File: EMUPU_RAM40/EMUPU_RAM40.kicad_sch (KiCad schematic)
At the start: 30 parts, among them J1 Conn_01x20_Socket, J2 Conn_01x20_Socket, J3 Barrel_Jack_Switch, J4 Conn_01x06_Pin, J5 Conn_01x08_Pin, SW1 SW_SPDT, SW2 SW_SPST, U1 PIC18F47Q43-IP, U2 628128

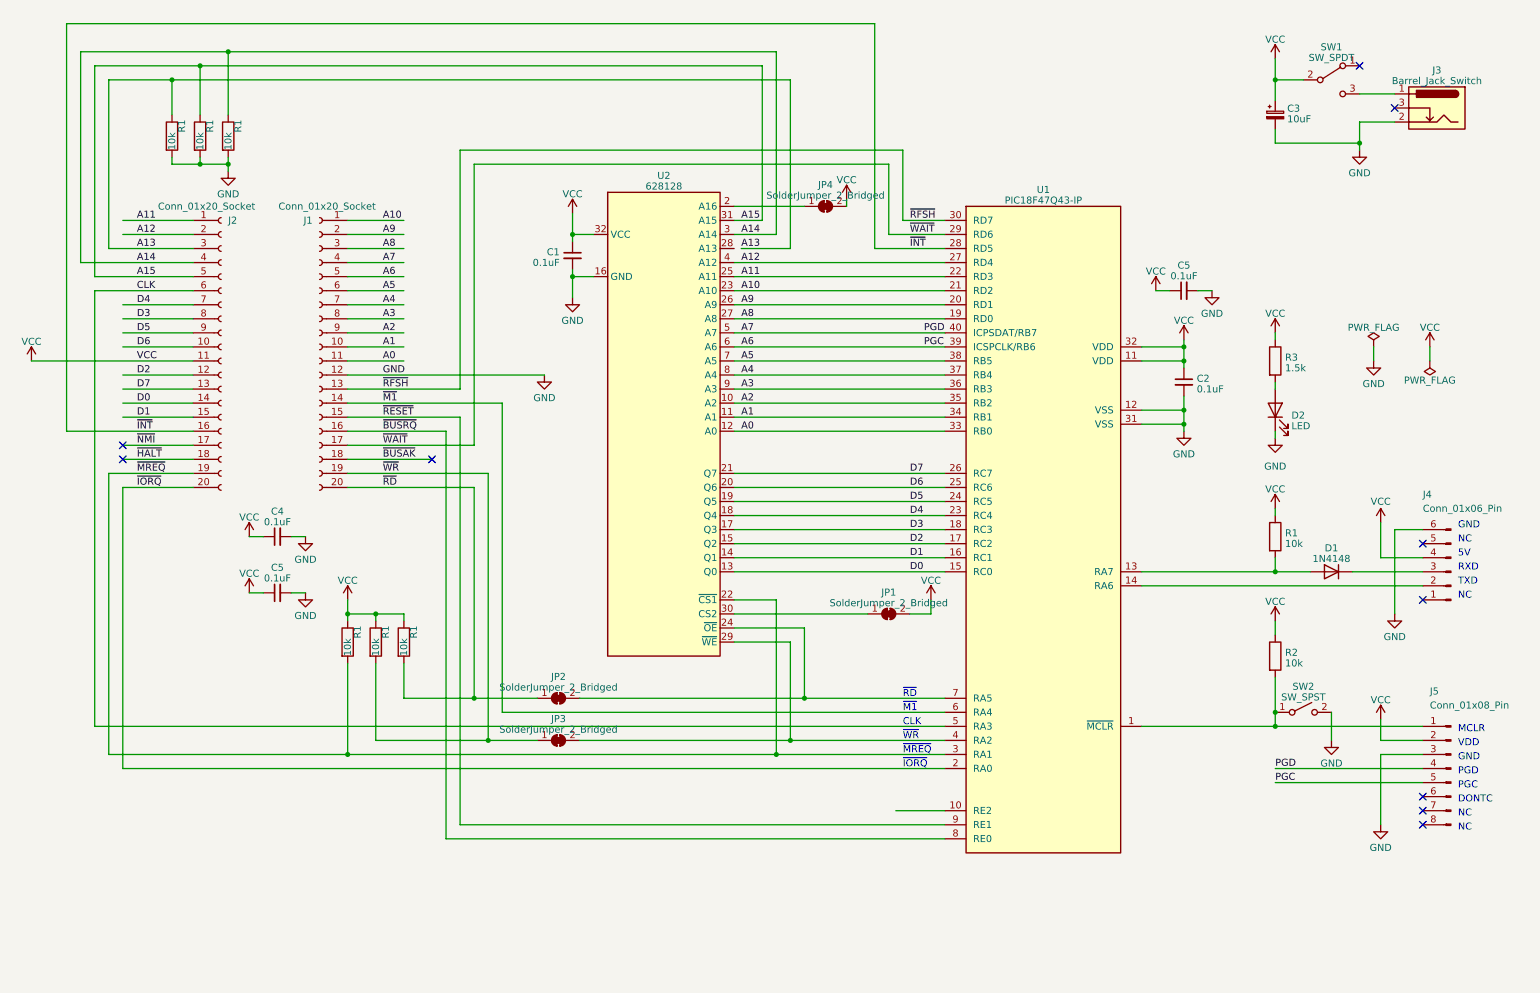
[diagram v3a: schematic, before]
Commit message: Rev003: arrange new footprints, before autorouting
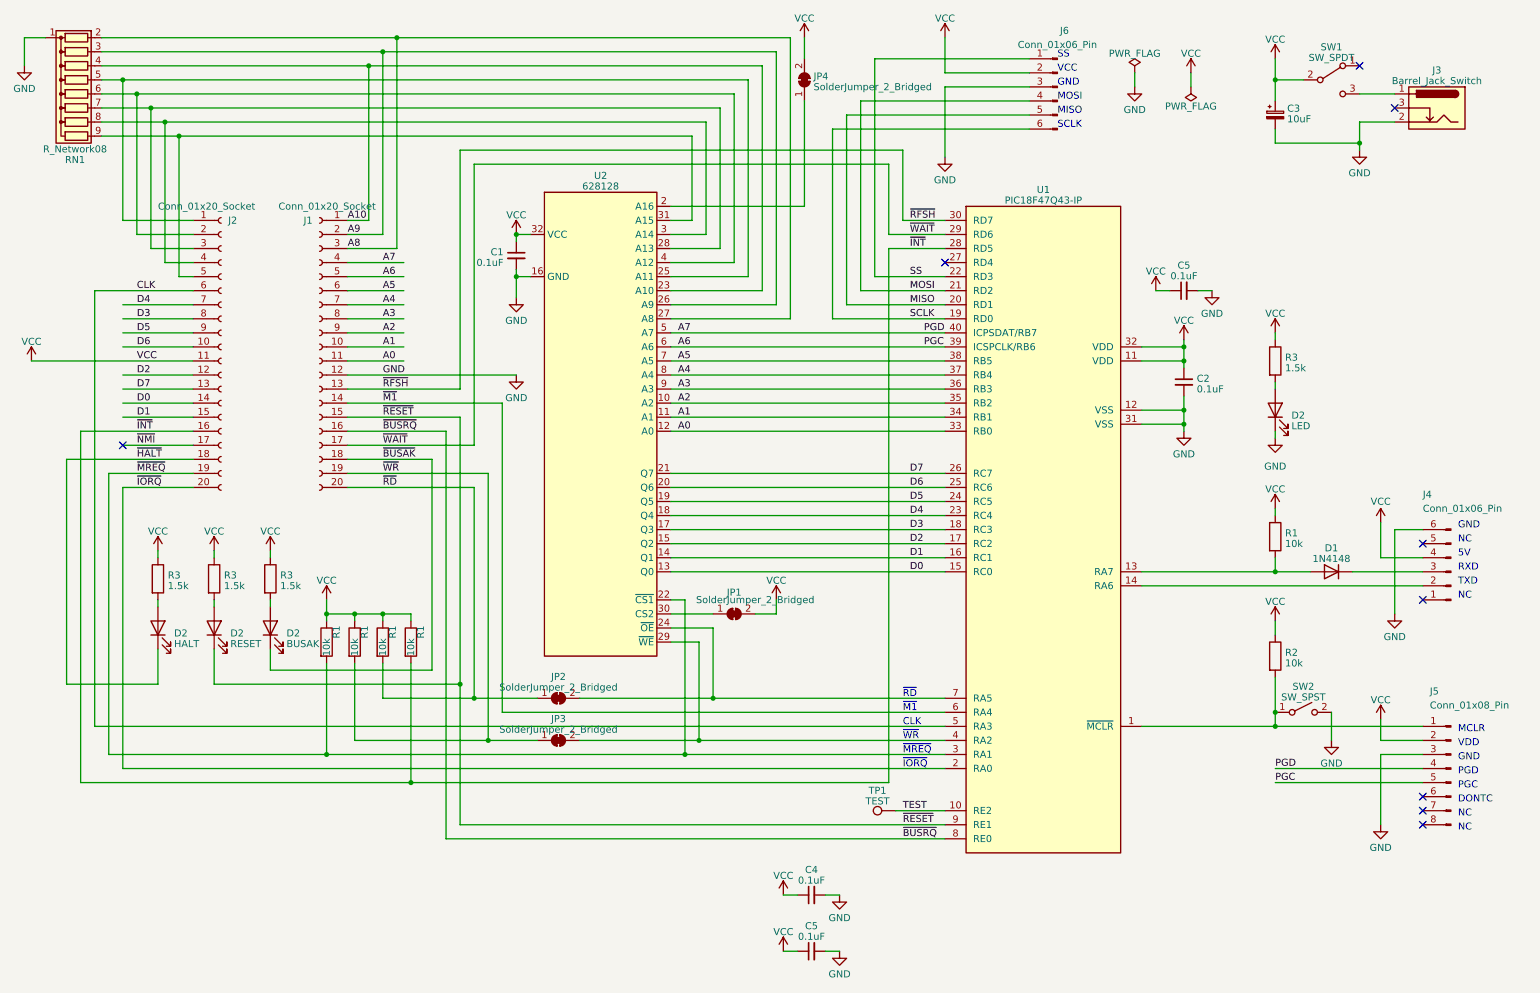
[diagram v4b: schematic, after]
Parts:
- removed R1 (x3): 10k, Resistor_THT:R_Axial_DIN0204_L3.6mm_D1.6mm_P7.62mm_Horizontal, symbol Device:R
- added D2: BUSAK, LED_THT:LED_D3.0mm, symbol Device:LED
- added D2: RESET, LED_THT:LED_D3.0mm, symbol Device:LED
- added D2: HALT, LED_THT:LED_D3.0mm, symbol Device:LED
- added J6: Conn_01x06_Pin, Connector_PinHeader_2.54mm:PinHeader_1x06_P2.54mm_Vertical, symbol Connector:Conn_01x06_Pin
- added R1: 10k, Resistor_THT:R_Axial_DIN0204_L3.6mm_D1.6mm_P7.62mm_Horizontal, symbol Device:R
- added R3 (x3): 1.5k, Resistor_THT:R_Axial_DIN0204_L3.6mm_D1.6mm_P7.62mm_Horizontal, symbol Device:R
- added RN1: R_Network08, Resistor_THT:R_Array_SIP9, symbol Device:R_Network08
- added TP1: TEST, Connector_PinHeader_2.54mm:PinHeader_1x01_P2.54mm_Vertical, symbol Connector:TestPoint
- J3: footprint 0-local:BARREL_JACK -> 0-Project:BARREL_JACK
- J4: footprint 0-local:PinHeader_1x06_P2.54mm_Horizontal_NoFeet -> 0-Project:PinHeader_1x06_P2.54mm_Horizontal_NoFeet
- J5: footprint 0-local:PinHeader_1x08_P2.54mm_Rev_Horizontal_Nofoot -> 0-Project:PinHeader_1x08_P2.54mm_Rev_Horizontal_Nofoot
- SW1: footprint 0-local:PowerSW_for_SBC_series -> 0-Project:PowerSW_for_SBC_series
- SW2: footprint 0-local:SW_PUSH_6mm_H4.3mm -> 0-Project:SW_PUSH_6mm_H4.3mm
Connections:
- net A13 is gone; now on an unnamed net: J2.3 (Pin_3)
- net A10: now also RN1.4 (R3); no longer U1.21 (RD2)
- net A8: now also RN1.2 (R1); no longer U1.19 (RD0)
- net A9: now also RN1.3 (R2); no longer U1.20 (RD1)
- net GND: now also J6.3 (Pin_3), RN1.1 (common)
- net VCC: now also J6.2 (Pin_2), R1.1, R3.1, R3.1, R3.1
- net ~{BUSAK}: now also D2.1 (K)
- net ~{HALT}: now also D2.1 (K)
- net ~{INT}: now also R1.2
- net ~{RESET}: now also D2.1 (K)
- net at U2.28 (A13): now also RN1.7 (R6)
- net TEST: now reaches U1.10 (RE2)
- net TEST: now also TP1.1
- net A11: no longer names the net of J2.1 (Pin_1), U2.25 (A11)
- net A11: now also RN1.5 (R4); no longer U1.22 (RD3)
- net A12: no longer names the net of J2.2 (Pin_2), U2.4 (A12)
- net A12: now also RN1.6 (R5); no longer U1.27 (RD4)
- net A14: no longer names the net of J2.4 (Pin_4), U2.3 (A14)
- net A14: now also RN1.8 (R7)
- net A15: no longer names the net of J2.5 (Pin_5), U2.31 (A15)
- net A15: now also RN1.9 (R8)
- new net: D2.2 (A), R3.2 (x3)
- new net MISO: J6.5 (Pin_5), U1.20 (RD1)
- new net MOSI: J6.4 (Pin_4), U1.21 (RD2)
- new net SCLK: J6.6 (Pin_6), U1.19 (RD0)
- new net SS: J6.1 (Pin_1), U1.22 (RD3)
- no-connect marks 10 -> 9
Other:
- note added: "MISO"
- note added: "MOSI"
- note added: "SCLK"
- note added: "SS"
- note added: "VCC"
- moved on the sheet: C1, C4, C5, JP1, JP4, R1, U2

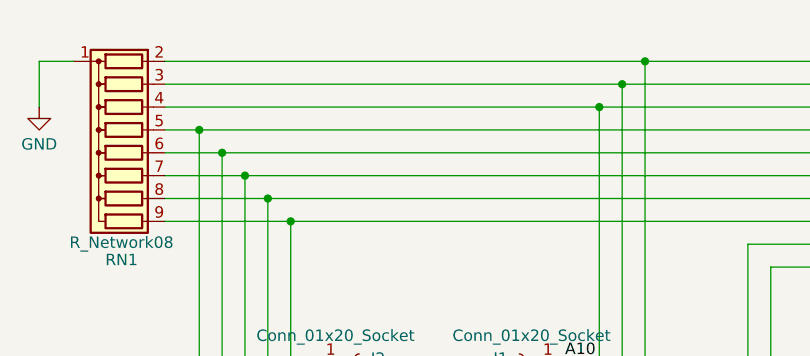
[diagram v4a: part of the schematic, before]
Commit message: Rev003: autorouting done, no no-connection, but some error/warning remains
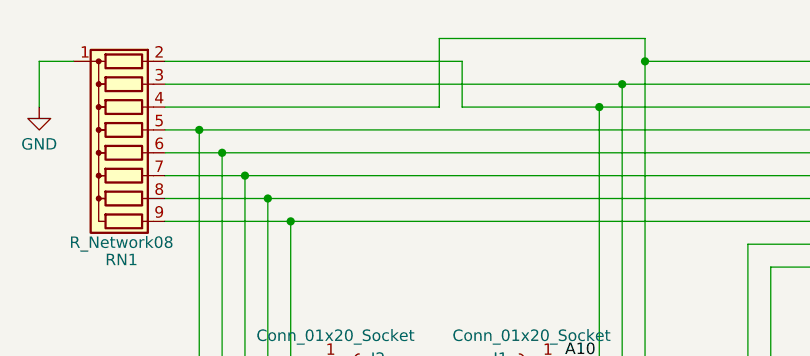
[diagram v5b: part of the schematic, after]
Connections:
- net A10: now also RN1.2 (R1); no longer RN1.4 (R3)
- net A8: now also RN1.4 (R3); no longer RN1.2 (R1)
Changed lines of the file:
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@@
   (junction (at 83.82 152.4) (diameter 0) (color 0 0 0 0)
   )
+  (junction (at 76.2 22.86) (diameter 0) (color 0 0 0 0)
+  )
   (junction (at 223.52 87.63) (diameter 0) (color 0 0 0 0)
   )
@@
   (junction (at 68.58 147.32) (diameter 0) (color 0 0 0 0)
   )
+  (junction (at 223.52 73.66) (diameter 0) (color 0 0 0 0)
+  )
+  (junction (at 255.27 36.83) (diameter 0) (color 0 0 0 0)
+  )
   (junction (at 81.28 17.78) (diameter 0) (color 0 0 0 0)
   )
-  (junction (at 223.52 73.66) (diameter 0) (color 0 0 0 0)
-  )
-  (junction (at 255.27 36.83) (diameter 0) (color 0 0 0 0)
-  )
   (junction (at 39.37 33.02) (diameter 0) (color 0 0 0 0)
   )
@@
   )
   (junction (at 135.89 144.78) (diameter 0) (color 0 0 0 0)
-  )
-  (junction (at 76.2 22.86) (diameter 0) (color 0 0 0 0)
   )
   (junction (at 73.66 121.92) (diameter 0) (color 0 0 0 0)
@@
     (stroke (width 0) (type default))
   )
+  (wire (pts (xy 27.94 22.86) (xy 58.42 22.86))
+    (stroke (width 0) (type default))
+  )
   (wire (pts (xy 90.17 162.56) (xy 180.34 162.56))
     (stroke (width 0) (type default))
@@
     (stroke (width 0) (type default))
   )
-  (wire (pts (xy 27.94 22.86) (xy 76.2 22.86))
-    (stroke (width 0) (type default))
-  )
   (wire (pts (xy 68.58 121.92) (xy 68.58 123.19))
     (stroke (width 0) (type default))
@@
     (stroke (width 0) (type default))
   )
+  (wire (pts (xy 76.2 22.86) (xy 60.96 22.86))
+    (stroke (width 0) (type default))
+  )
   (wire (pts (xy 72.39 81.28) (xy 92.71 81.28))
     (stroke (width 0) (type default))
@@
     (stroke (width 0) (type default))
   )
+  (wire (pts (xy 58.42 15.24) (xy 81.28 15.24))
+    (stroke (width 0) (type default))
+  )
   (wire (pts (xy 24.13 88.9) (xy 44.45 88.9))
     (stroke (width 0) (type default))
@@
     (stroke (width 0) (type default))
   )
+  (wire (pts (xy 58.42 22.86) (xy 58.42 15.24))
+    (stroke (width 0) (type default))
+  )
   (wire (pts (xy 48.26 110.49) (xy 48.26 111.76))
     (stroke (width 0) (type default))
@@
     (stroke (width 0) (type default))
   )
-  (wire (pts (xy 27.94 17.78) (xy 81.28 17.78))
-    (stroke (width 0) (type default))
-  )
   (wire (pts (xy 73.66 121.92) (xy 73.66 123.19))
     (stroke (width 0) (type default))
@@
     (stroke (width 0) (type default))
   )
+  (wire (pts (xy 60.96 17.78) (xy 60.96 22.86))
+    (stroke (width 0) (type default))
+  )
   (wire (pts (xy 130.81 81.28) (xy 180.34 81.28))
     (stroke (width 0) (type default))
@@
     (stroke (width 0) (type default))
   )
+  (wire (pts (xy 27.94 17.78) (xy 60.96 17.78))
+    (stroke (width 0) (type default))
+  )
   (wire (pts (xy 92.71 160.02) (xy 180.34 160.02))
     (stroke (width 0) (type default))
@@
     (stroke (width 0) (type default))
   )
+  (wire (pts (xy 81.28 15.24) (xy 81.28 17.78))
+    (stroke (width 0) (type default))
+  )

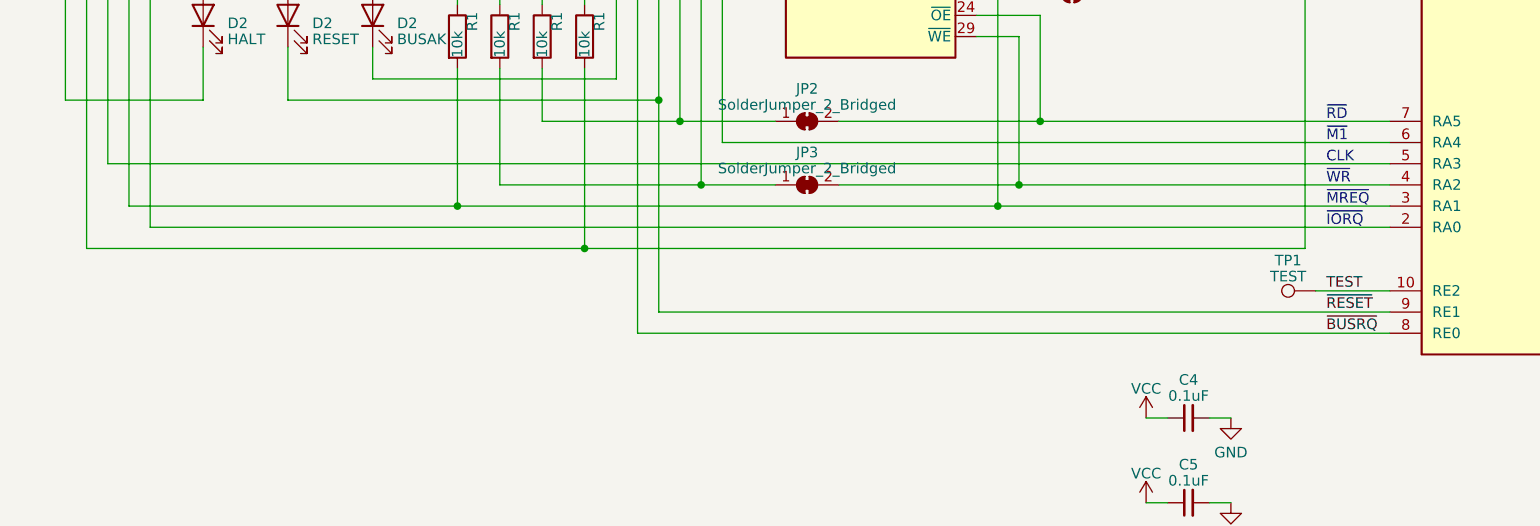
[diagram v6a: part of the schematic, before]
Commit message: Rev004, add 10k pullup resister to IORQ
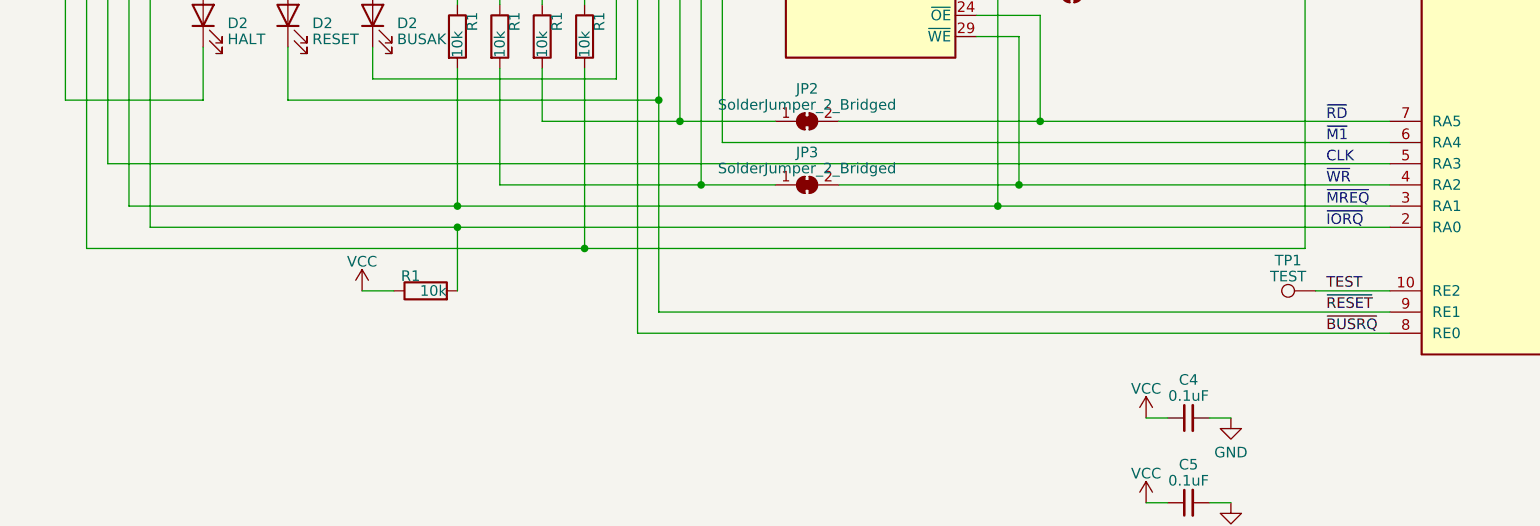
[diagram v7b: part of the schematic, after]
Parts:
- added R1: 10k, Resistor_THT:R_Axial_DIN0204_L3.6mm_D1.6mm_P7.62mm_Horizontal, symbol Device:R
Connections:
- net VCC: now also R1.1
- net ~{IORQ}: now also R1.2
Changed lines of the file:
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@@
   (junction (at 240.03 25.4) (diameter 0) (color 0 0 0 0)
   )
+  (junction (at 68.58 149.86) (diameter 0) (color 0 0 0 0)
+  )
   (junction (at 102.87 60.96) (diameter 0) (color 0 0 0 0)
   )
@@
     (stroke (width 0) (type default))
   )
+  (wire (pts (xy 68.58 149.86) (xy 180.34 149.86))
+    (stroke (width 0) (type default))
+  )
   (wire (pts (xy 27.94 22.86) (xy 58.42 22.86))
     (stroke (width 0) (type default))
@@
     (stroke (width 0) (type default))
   )
+  (wire (pts (xy 57.15 157.48) (xy 60.96 157.48))
+    (stroke (width 0) (type default))
+  )
   (wire (pts (xy 130.81 76.2) (xy 180.34 76.2))
     (stroke (width 0) (type default))
@@
     (stroke (width 0) (type default))
   )
-  (wire (pts (xy 31.75 149.86) (xy 180.34 149.86))
+  (wire (pts (xy 31.75 149.86) (xy 68.58 149.86))
     (stroke (width 0) (type default))
   )
@@
     (stroke (width 0) (type default))
   )
+  (wire (pts (xy 68.58 149.86) (xy 68.58 157.48))
+    (stroke (width 0) (type default))
+  )
   (text "MISO" (at 200.66 31.75 0)
     (effects (font (size 1.27 1.27)) (justify left bottom))
@@
     )
   )
+  (symbol (lib_id "Device:R") (at 64.77 157.48 90) (unit 1)
+    (in_bom yes) (on_board yes) (dnp no)
+    (property "Reference" "R1" (at 64.1263 155.702 90)
+      (effects (font (size 1.27 1.27)) (justify left))
+    )
+    (property "Value" "10k" (at 67.31 157.48 90)
+      (effects (font (size 1.27 1.27)) (justify left))
+    )
+    (property "Footprint" "Resistor_THT:R_Axial_DIN0204_L3.6mm_D1.6mm_P7.62mm_Horizontal" (at 64.77 159.258 90)
+      (effects (font (size 1.27 1.27)) hide)
+    )
+    (property "Datasheet" "~" (at 64.77 157.48 0)
+      (effects (font (size 1.27 1.27)) hide)
+    )
+    (pin "1")
+    (pin "2")
+    (instances
+      (project "EMUPU_RAM"
+        (path "/6d2188b2-a6ec-4341-9e2f-19ddbe5554d2"
+          (reference "R1") (unit 1)
+        )
+      )
+      (project "EMUPU_RAM40"
+        (path "/e6d6b00c-3eac-46b2-864a-d30920c7bbcf"
+          (reference "R11") (unit 1)
+        )
+      )
+    )
+  )
   (symbol (lib_id "Device:R_Network08") (at 22.86 27.94 90) (mirror x) (unit 1)
     (in_bom yes) (on_board yes) (dnp no)
@@
         )
       )
+    )
+  )
+  (symbol (lib_id "power:VCC") (at 57.15 157.48 0) (mirror y) (unit 1)
+    (in_bom yes) (on_board yes) (dnp no)
+    (property "Reference" "#PWR024" (at 57.15 161.29 0)
+      (effects (font (size 1.27 1.27)) hide)
+    )
+    (property "Value" "VCC" (at 57.15 153.9781 0)
+      (effects (font (size 1.27 1.27)))
+    )
+    (property "Footprint" "" (at 57.15 157.48 0)
+      (effects (font (size 1.27 1.27)) hide)
+    )
+    (property "Datasheet" "" (at 57.15 157.48 0)
+      (effects (font (size 1.27 1.27)) hide)
+    )
+    (pin "1")
+    (instances
+      (project "EMUPU_RAM"
+        (path "/6d2188b2-a6ec-4341-9e2f-19ddbe5554d2"
+          (reference "#PWR024") (unit 1)
+        )
+      )
+      (project "EMUPU_RAM40"
+        (path "/e6d6b00c-3eac-46b2-864a-d30920c7bbcf"
+          (reference "#PWR033") (unit 1)
+        )
+      )
